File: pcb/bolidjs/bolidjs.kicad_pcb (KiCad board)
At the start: 2 copper layers, 103.9 x 52.6 mm, 62 parts, among them J1 Vext, J11 rearL+, J12 rearL-, J13 rearR+, J14 rearR-, J17 frontL, J18 f1L, J19 f2L, J20 frontR, J21 f1R, J22 f2R, J23 frontBar, J24 VCC, J25 D14, J26 D29, J27 D15, J28 D31, J3 FL, J34 BM, J35 BM, J36 VDD, J4 FR, J5 F, J6 END1, J7 END1, J8 END2, J9 END2, M1 Stepper, U1 MDB42Q_brkout, U2 LB1930MC-AH, U3 LB1930MC-AH, U4 LB1930MC-AH, U5 LB1930MC-AH

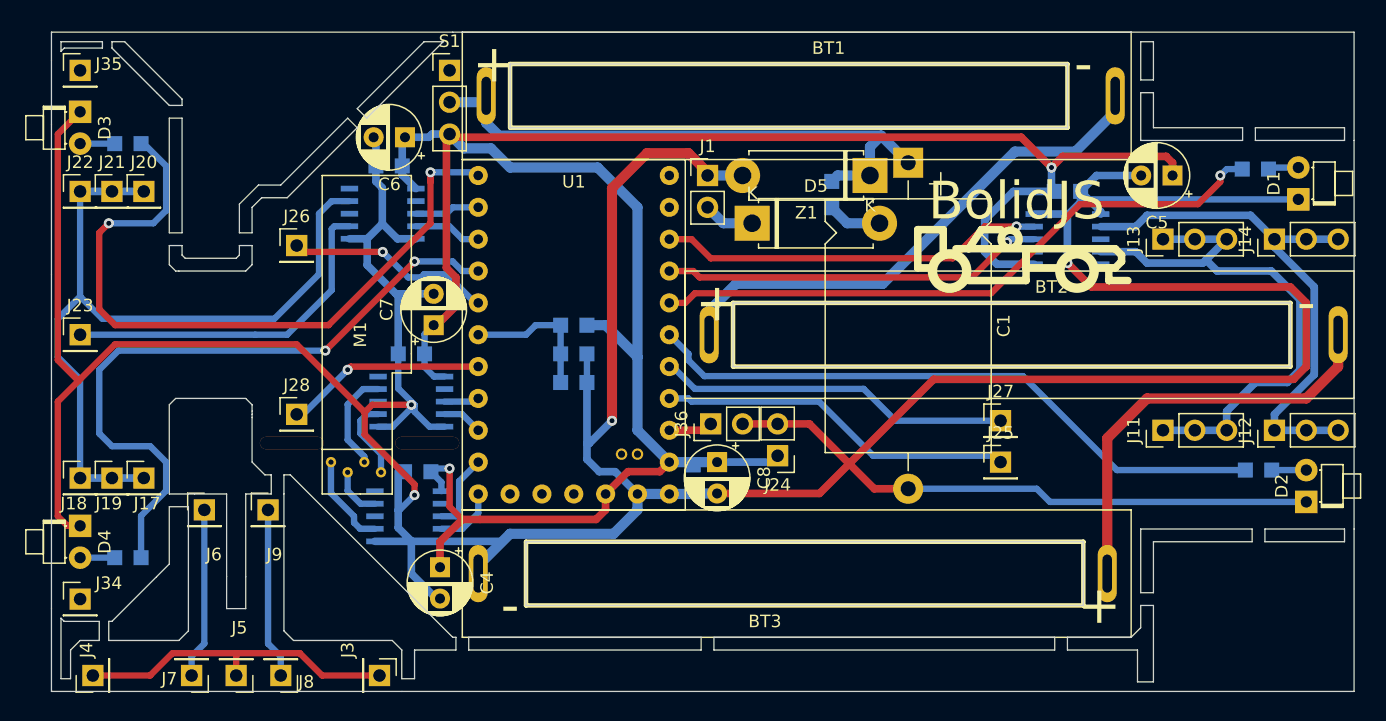
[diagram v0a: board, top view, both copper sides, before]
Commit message: added steering option and wheel pads
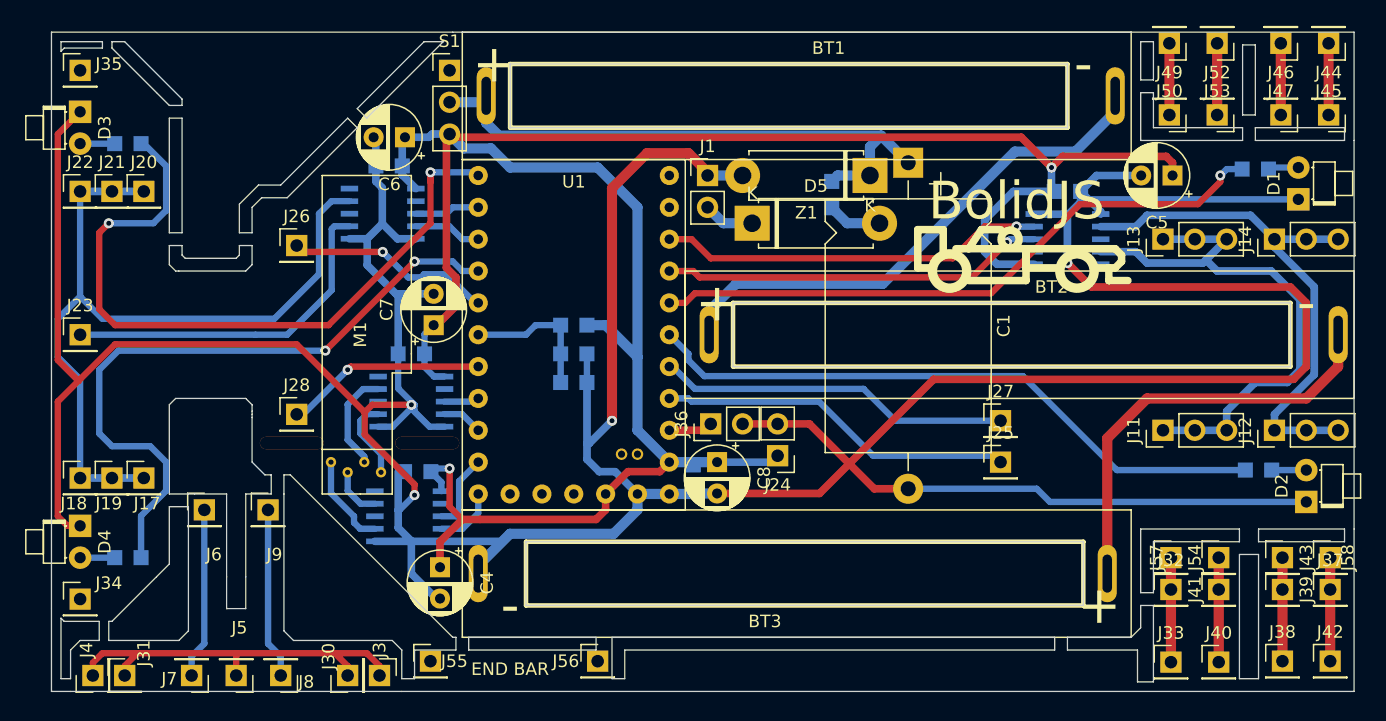
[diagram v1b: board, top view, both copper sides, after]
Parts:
- added J30: FL, Connector_PinHeader_2.54mm:PinHeader_1x01_P2.54mm_Vertical, F.Cu at (97.5, 103.4)
- added J31: FR, Connector_PinHeader_2.54mm:PinHeader_1x01_P2.54mm_Vertical, F.Cu at (79.8, 103.4)
- added J32: FL, Connector_PinHeader_2.54mm:PinHeader_1x01_P2.54mm_Vertical, F.Cu at (163.2, 96.5)
- added J33: FL, Connector_PinHeader_2.54mm:PinHeader_1x01_P2.54mm_Vertical, F.Cu at (163.2, 102.3)
- added J37: FL, Connector_PinHeader_2.54mm:PinHeader_1x01_P2.54mm_Vertical, F.Cu at (175.9, 96.5)
- added J38: FL, Connector_PinHeader_2.54mm:PinHeader_1x01_P2.54mm_Vertical, F.Cu at (172.1, 102.2)
- added J39: FL, Connector_PinHeader_2.54mm:PinHeader_1x01_P2.54mm_Vertical, F.Cu at (172.1, 96.5)
- added J40: FL, Connector_PinHeader_2.54mm:PinHeader_1x01_P2.54mm_Vertical, F.Cu at (167.0, 102.3)
- added J41: FL, Connector_PinHeader_2.54mm:PinHeader_1x01_P2.54mm_Vertical, F.Cu at (167.0, 96.5)
- added J42: FL, Connector_PinHeader_2.54mm:PinHeader_1x01_P2.54mm_Vertical, F.Cu at (175.9, 102.2)
- added J43: FL, Connector_PinHeader_2.54mm:PinHeader_1x01_P2.54mm_Vertical, F.Cu at (172.1, 94.0)
- added J44: FL, Connector_PinHeader_2.54mm:PinHeader_1x01_P2.54mm_Vertical, F.Cu at (175.8, 53.0)
- added J45: FL, Connector_PinHeader_2.54mm:PinHeader_1x01_P2.54mm_Vertical, F.Cu at (175.8, 58.7)
- added J46: FL, Connector_PinHeader_2.54mm:PinHeader_1x01_P2.54mm_Vertical, F.Cu at (172.0, 53.0)
- added J47: FL, Connector_PinHeader_2.54mm:PinHeader_1x01_P2.54mm_Vertical, F.Cu at (172.0, 58.7)
- added J49: FL, Connector_PinHeader_2.54mm:PinHeader_1x01_P2.54mm_Vertical, F.Cu at (163.1, 53.0)
- added J50: FL, Connector_PinHeader_2.54mm:PinHeader_1x01_P2.54mm_Vertical, F.Cu at (163.1, 58.7)
- added J52: FL, Connector_PinHeader_2.54mm:PinHeader_1x01_P2.54mm_Vertical, F.Cu at (166.9, 53.0)
- added J53: FL, Connector_PinHeader_2.54mm:PinHeader_1x01_P2.54mm_Vertical, F.Cu at (166.9, 58.7)
- added J54: FL, Connector_PinHeader_2.54mm:PinHeader_1x01_P2.54mm_Vertical, F.Cu at (167.0, 94.0)
- added J55: FL, Connector_PinHeader_2.54mm:PinHeader_1x01_P2.54mm_Vertical, F.Cu at (104.1, 102.2)
- added J56: FL, Connector_PinHeader_2.54mm:PinHeader_1x01_P2.54mm_Vertical, F.Cu at (117.5, 102.2)
- added J57: FL, Connector_PinHeader_2.54mm:PinHeader_1x01_P2.54mm_Vertical, F.Cu at (163.2, 94.0)
- added J58: FL, Connector_PinHeader_2.54mm:PinHeader_1x01_P2.54mm_Vertical, F.Cu at (175.9, 94.0)
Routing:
- net Net-(J32-Pad1): track 0.00 -> 8.33 mm
- net Net-(J40-Pad1): track 0.00 -> 8.33 mm
- net Net-(J38-Pad1): track 0.00 -> 8.25 mm
- net Net-(J37-Pad1): track 0.00 -> 8.25 mm
- net Net-(J52-Pad1): track 0.00 -> 5.71 mm
- net Net-(J49-Pad1): track 0.00 -> 5.71 mm
- net Net-(J46-Pad1): track 0.00 -> 5.71 mm
- net Net-(J44-Pad1): track 0.00 -> 5.71 mm
- net Net-(J3-Pad1): track 26.1 -> 31.6 mm
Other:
- outline, holes or cut-outs redrawn
- board text added: "END BAR"

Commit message: removed options for motor sizes
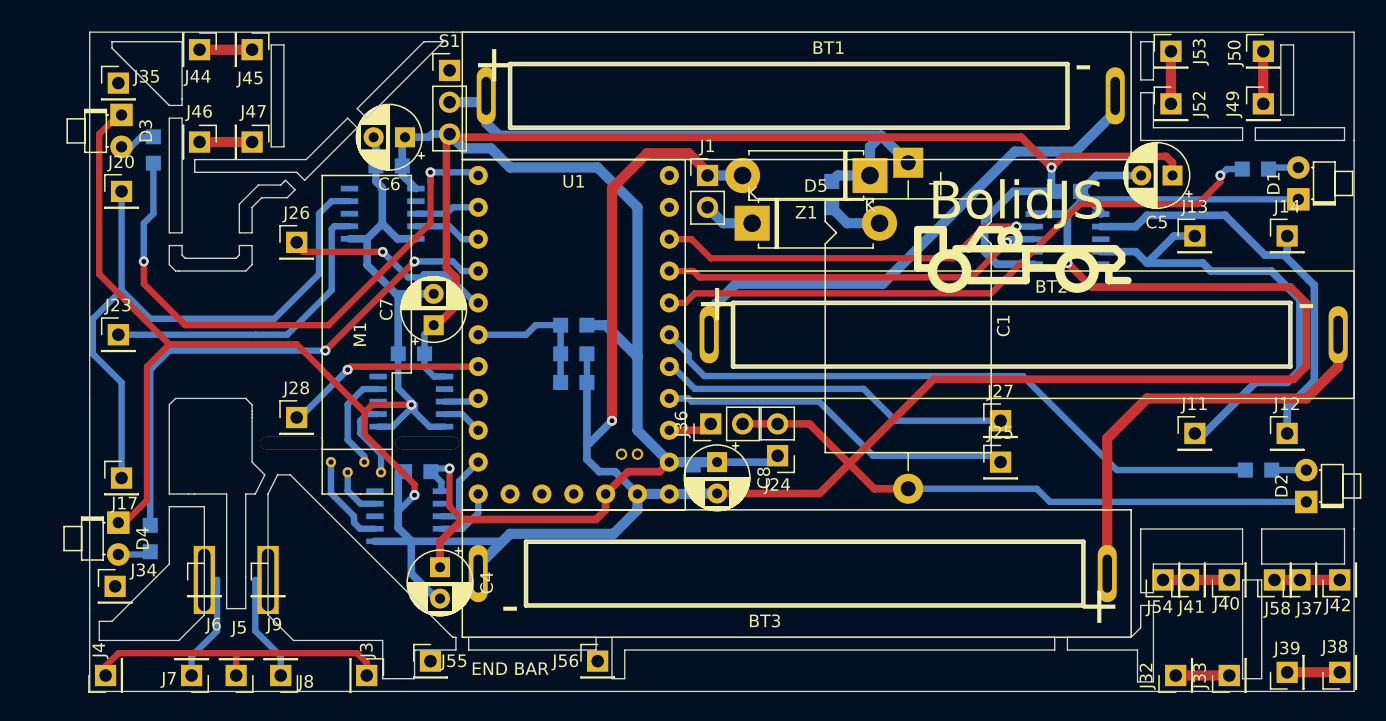
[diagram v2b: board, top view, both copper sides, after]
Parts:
- removed J18: f1L, Connector_PinHeader_2.54mm:PinHeader_1x01_P2.54mm_Vertical
- removed J19: f2L, Connector_PinHeader_2.54mm:PinHeader_1x01_P2.54mm_Vertical
- removed J21: f1R, Connector_PinHeader_2.54mm:PinHeader_1x01_P2.54mm_Vertical
- removed J22: f2R, Connector_PinHeader_2.54mm:PinHeader_1x01_P2.54mm_Vertical
- removed J30, J43, J57: FL, Connector_PinHeader_2.54mm:PinHeader_1x01_P2.54mm_Vertical
- removed J31: FR, Connector_PinHeader_2.54mm:PinHeader_1x01_P2.54mm_Vertical
- J11, J12, J13, J14: footprint Connector_PinHeader_2.54mm:PinHeader_1x03_P2.54mm_Vertical -> Connector_PinHeader_2.54mm:PinHeader_1x01_P2.54mm_Vertical
- moved J44 90.0 mm to (85.7, 53.5), turned to 270 degrees
- moved J46 86.6 mm to (85.7, 60.8), turned to 270 degrees
- moved J45 86.0 mm to (89.9, 53.5), turned to 270 degrees
- moved J47 82.1 mm to (89.9, 60.8), turned to 270 degrees
- moved J50 9.05 mm to (170.6, 53.6), turned to 0 degrees
- moved J49 8.91 mm to (170.6, 57.8), turned to 0 degrees
- moved J32 6.87 mm to (163.6, 103.4), turned to 90 degrees
- moved J39 6.61 mm to (172.5, 103.1), turned to 90 degrees
- moved J40 6.61 mm to (167.8, 95.8), turned to 90 degrees
- moved J42 6.52 mm to (176.7, 95.8), turned to 90 degrees
- moved J53 6.27 mm to (163.2, 53.6), turned to 0 degrees
- moved J52 6.07 mm to (163.2, 57.8), turned to 0 degrees
- moved J6 5.59 mm to (86.1, 95.8)
- moved J9 5.59 mm to (91.2, 95.8)
- moved J58 4.79 mm to (171.4, 95.8), turned to 90 degrees
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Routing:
- net Net-(J17-Pad1): track 63.4 -> 50.6 mm
- net /D28: track 53.9 -> 42.5 mm
- net /D25: track 57.3 -> 46.0 mm
- net Net-(J12-Pad1): track 43.1 -> 34.1 mm
- net GND: track 366.6 -> 359.4 mm
- net Net-(J3-Pad1): track 31.6 -> 25.1 mm
- net Net-(J11-Pad1): track 44.5 -> 38.3 mm
- net Net-(J8-Pad1): track 13.6 -> 9.00 mm
- net Net-(J6-Pad1): track 13.6 -> 9.48 mm
- net Net-(J38-Pad1): track 8.25 -> 4.19 mm
- net Net-(J32-Pad1): track 8.33 -> 4.27 mm
- net Net-(J40-Pad1): track 8.33 -> 5.28 mm
- net Net-(J23-Pad1): track 27.9 -> 24.9 mm
- net Net-(J37-Pad1): track 8.25 -> 5.21 mm
- net Net-(J52-Pad1): track 5.71 -> 4.19 mm
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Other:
- board size 103.9 x 52.6 mm -> 100.8 x 52.6 mm

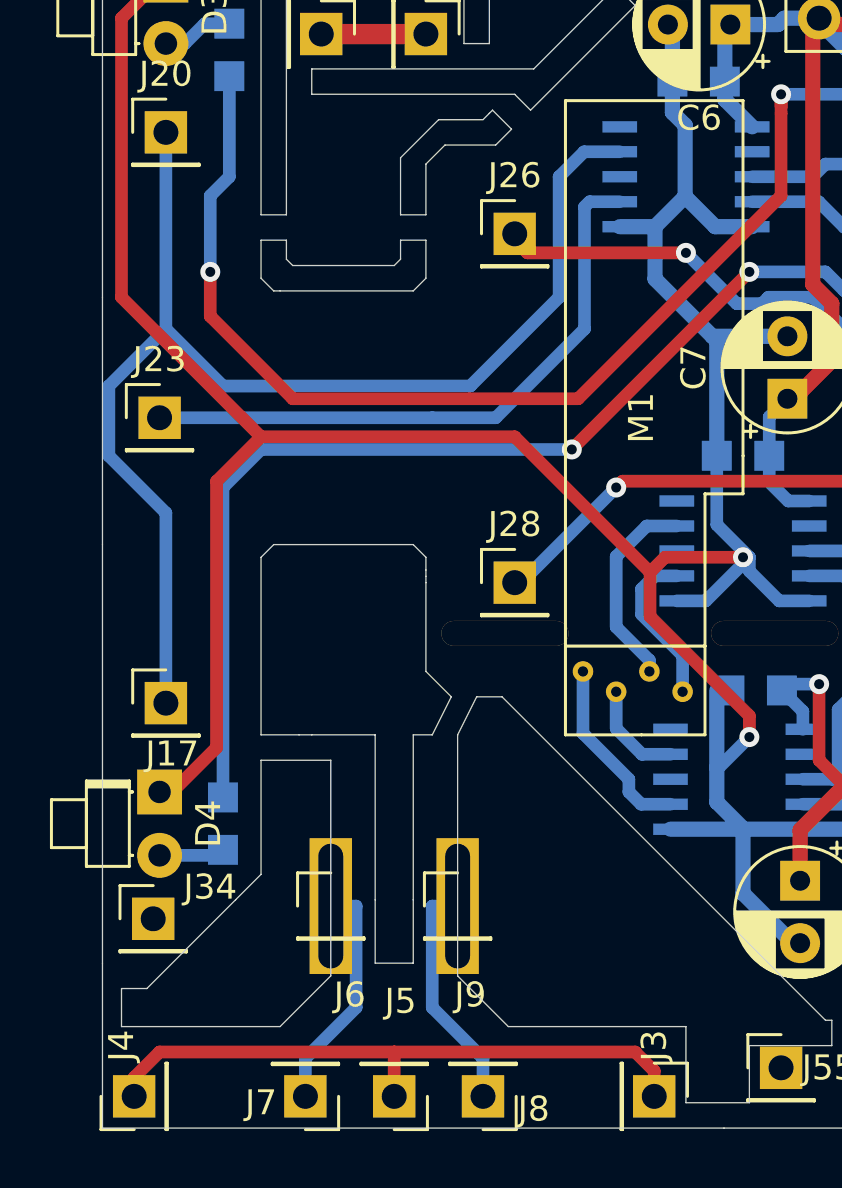
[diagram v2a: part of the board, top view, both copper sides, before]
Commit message: steering bar is ticker
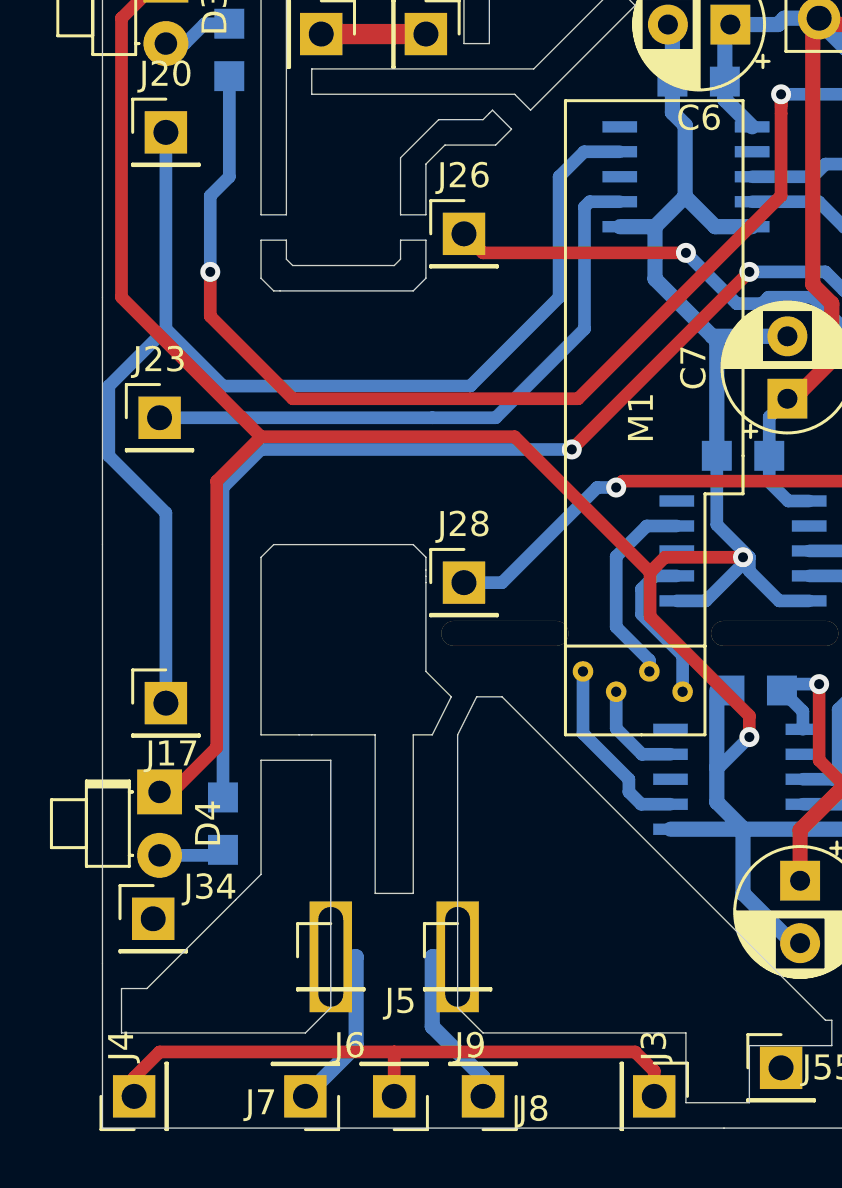
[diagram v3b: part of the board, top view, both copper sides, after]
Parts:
- moved J6 2.03 mm to (86.1, 97.8)
- moved J9 2.03 mm to (91.2, 97.8)
- moved J26 2.03 mm to (91.4, 68.8)
- moved J28 2.03 mm to (91.4, 82.8)
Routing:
- net Net-(J6-Pad1): track 9.48 -> 7.45 mm
- net /D31: track 16.2 -> 18.2 mm
- net /D29: track 16.8 -> 18.7 mm
- net Net-(J8-Pad1): track 9.00 -> 7.95 mm
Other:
- outline, holes or cut-outs redrawn

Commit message: minor change
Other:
- board text added: "ON/OFF"
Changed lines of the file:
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@@
   (general
     (thickness 1.6)
-    (drawings 250)
+    (drawings 244)
     (tracks 394)
     (zones 0)
@@
     (34 B.Paste user)
     (35 F.Paste user)
-    (36 B.SilkS user hide)
+    (36 B.SilkS user)
     (37 F.SilkS user)
     (38 B.Mask user)
@@
       (padsonsilk false)
       (subtractmaskfromsilk false)
-      (outputformat 4)
+      (outputformat 1)
       (mirror false)
       (drillshape 0)
@@
     )
   )
-  (dimension 4.572 (width 0.15) (layer Dwgs.User)
-    (gr_text "4.572 mm" (at 96.296 101.092 90) (layer Dwgs.User)
-      (effects (font (size 1 1) (thickness 0.15)))
-    )
-    (feature1 (pts (xy 92.456 98.806) (xy 95.582421 98.806)))
-    (feature2 (pts (xy 92.456 103.378) (xy 95.582421 103.378)))
-    (crossbar (pts (xy 94.996 103.378) (xy 94.996 98.806)))
-    (arrow1a (pts (xy 94.996 98.806) (xy 95.582421 99.932504)))
-    (arrow1b (pts (xy 94.996 98.806) (xy 94.409579 99.932504)))
-    (arrow2a (pts (xy 94.996 103.378) (xy 95.582421 102.251496)))
-    (arrow2b (pts (xy 94.996 103.378) (xy 94.409579 102.251496)))
-  )
-  (dimension 4.572 (width 0.15) (layer Dwgs.User)
-    (gr_text "4.572 mm" (at 89.154 80.234) (layer Dwgs.User)
-      (effects (font (size 1 1) (thickness 0.15)))
-    )
-    (feature1 (pts (xy 86.868 82.804) (xy 86.868 80.947579)))
-    (feature2 (pts (xy 91.44 82.804) (xy 91.44 80.947579)))
-    (crossbar (pts (xy 91.44 81.534) (xy 86.868 81.534)))
-    (arrow1a (pts (xy 86.868 81.534) (xy 87.994504 80.947579)))
-    (arrow1b (pts (xy 86.868 81.534) (xy 87.994504 82.120421)))
-    (arrow2a (pts (xy 91.44 81.534) (xy 90.313496 80.947579)))
-    (arrow2b (pts (xy 91.44 81.534) (xy 90.313496 82.120421)))
-  )
-  (dimension 20.828 (width 0.15) (layer Dwgs.User)
-    (gr_text "20.828 mm" (at 88.646 107.726) (layer Dwgs.User)
-      (effects (font (size 1 1) (thickness 0.15)))
-    )
-    (feature1 (pts (xy 99.06 103.378) (xy 99.06 107.012421)))
-    (feature2 (pts (xy 78.232 103.378) (xy 78.232 107.012421)))
-    (crossbar (pts (xy 78.232 106.426) (xy 99.06 106.426)))
-    (arrow1a (pts (xy 99.06 106.426) (xy 97.933496 107.012421)))
-    (arrow1b (pts (xy 99.06 106.426) (xy 97.933496 105.839579)))
-    (arrow2a (pts (xy 78.232 106.426) (xy 79.358504 107.012421)))
-    (arrow2b (pts (xy 78.232 106.426) (xy 79.358504 105.839579)))
-  )
-  (dimension 22.86 (width 0.15) (layer Dwgs.User)
-    (gr_text "22.860 mm" (at 73.884 76.2 270) (layer Dwgs.User)
-      (effects (font (size 1 1) (thickness 0.15)))
-    )
-    (feature1 (pts (xy 79.502 87.63) (xy 74.597579 87.63)))
-    (feature2 (pts (xy 79.502 64.77) (xy 74.597579 64.77)))
-    (crossbar (pts (xy 75.184 64.77) (xy 75.184 87.63)))
-    (arrow1a (pts (xy 75.184 87.63) (xy 74.597579 86.503496)))
-    (arrow1b (pts (xy 75.184 87.63) (xy 75.770421 86.503496)))
-    (arrow2a (pts (xy 75.184 64.77) (xy 74.597579 65.896504)))
-    (arrow2b (pts (xy 75.184 64.77) (xy 75.770421 65.896504)))
-  )
-  (dimension 1.016 (width 0.15) (layer Dwgs.User)
-    (gr_text "1.016 mm" (at 90.2 87.122 90) (layer Dwgs.User)
-      (effects (font (size 1 1) (thickness 0.15)))
-    )
-    (feature1 (pts (xy 86.868 86.614) (xy 89.486421 86.614)))
-    (feature2 (pts (xy 86.868 87.63) (xy 89.486421 87.63)))
-    (crossbar (pts (xy 88.9 87.63) (xy 88.9 86.614)))
-    (arrow1a (pts (xy 88.9 86.614) (xy 89.486421 87.740504)))
-    (arrow1b (pts (xy 88.9 86.614) (xy 88.313579 87.740504)))
-    (arrow2a (pts (xy 88.9 87.63) (xy 89.486421 86.503496)))
-    (arrow2b (pts (xy 88.9 87.63) (xy 88.313579 86.503496)))
-  )
-  (dimension 7.366 (width 0.15) (layer Dwgs.User)
-    (gr_text "7.366 mm" (at 83.185 83.028) (layer Dwgs.User)
-      (effects (font (size 1 1) (thickness 0.15)))
-    )
-    (feature1 (pts (xy 86.868 87.63) (xy 86.868 83.741579)))
-    (feature2 (pts (xy 79.502 87.63) (xy 79.502 83.741579)))
-    (crossbar (pts (xy 79.502 84.328) (xy 86.868 84.328)))
-    (arrow1a (pts (xy 86.868 84.328) (xy 85.741496 84.914421)))
-    (arrow1b (pts (xy 86.868 84.328) (xy 85.741496 83.741579)))
-    (arrow2a (pts (xy 79.502 84.328) (xy 80.628504 84.914421)))
-    (arrow2b (pts (xy 79.502 84.328) (xy 80.628504 83.741579)))
+  (gr_text ON/OFF (at 103.886 57.404 90) (layer F.SilkS)
+    (effects (font (size 1 1) (thickness 0.15)))
   )
-  (gr_line (start 168.91 76.2) (end 79.502 87.63) (layer Dwgs.User) (width 0.15))
   (gr_line (start 93.345 64.643) (end 92.71 65.278) (layer Edge.Cuts) (width 0.05))
   (gr_line (start 92.583 63.881) (end 92.456 64.008) (layer Edge.Cuts) (width 0.05))
